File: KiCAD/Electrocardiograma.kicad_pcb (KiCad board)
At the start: 2 copper layers, 56.5 x 47.2 mm, 76 parts, among them J1 54-00174, J2 Conn_01x02_Pin, J3 USB_C_Receptacle_PowerOnly_6P, J4 Conn_01x02_Pin, J5 Conn_01x02_Pin, J6 Conn_01x04_Pin, U1 INA823DT, U2 ESP32-C3-WROOM-02, U3 TLV1117-33, U4 TLV4888, U5 TLV4888, U6 TLV1117-ADJ, U7 SC6038, U8 CH224K

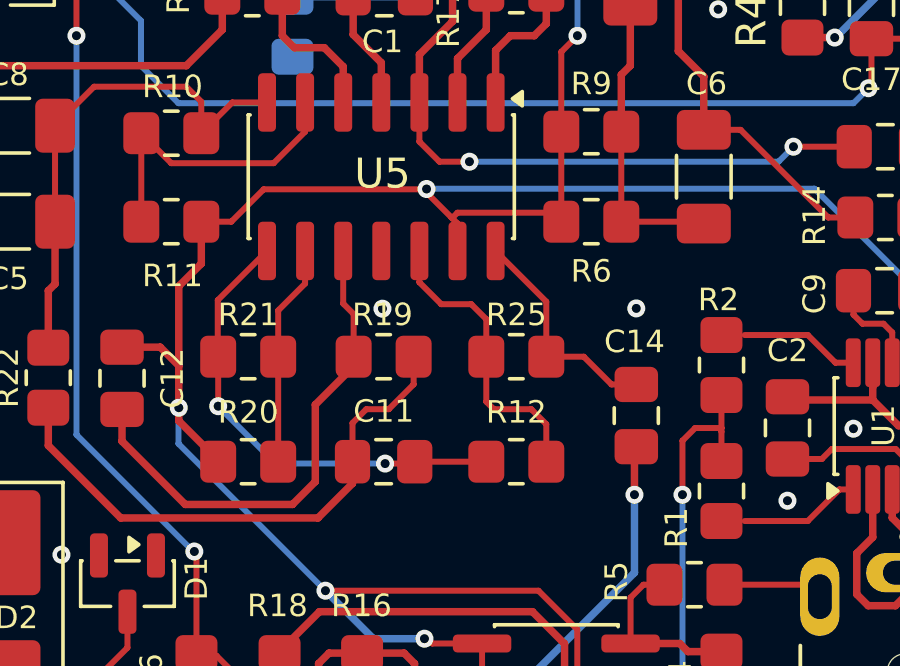
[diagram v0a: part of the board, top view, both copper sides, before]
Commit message: Corrección opamp
Corregido un opamp mal trazado en el esquematico y pcb
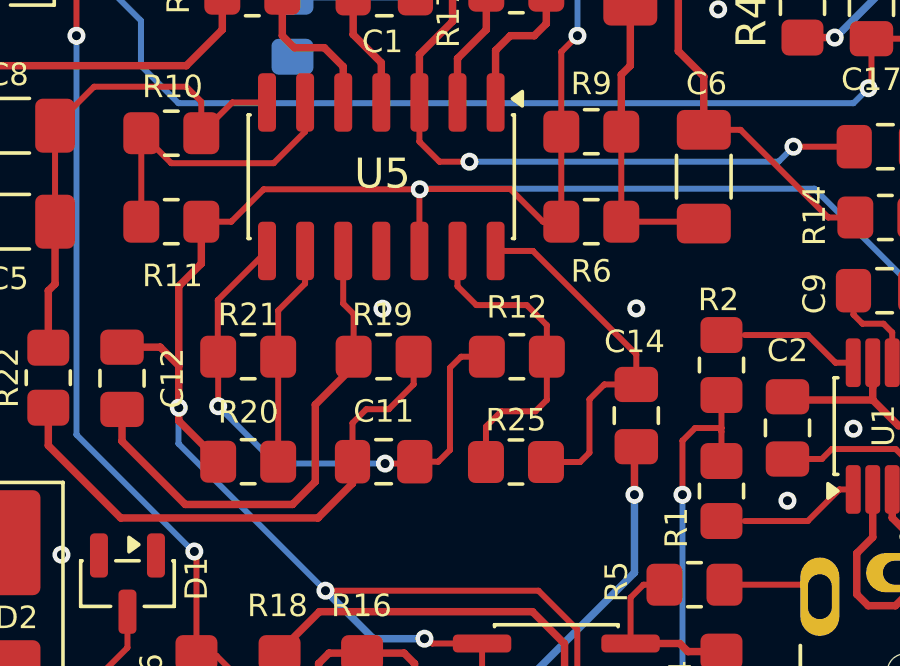
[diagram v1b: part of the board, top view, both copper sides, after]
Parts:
- moved R25 3.51 mm to (162.2, 104.2)
- moved R12 3.50 mm to (162.3, 100.7)
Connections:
- R12 pad 2: Net-(U5D-+) -> Net-(U5D--)
- R25 pad 1: Net-(U5D-+) -> Net-(U5D--)
- U5 pad 12: Net-(U5D-+) -> GND
- U5 pad 13: GND -> Net-(U5D--)
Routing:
- net Net-(U5D--): track 0.00 -> 10.8 mm
- net Net-(U5D-+): track 10.6 -> 0.00 mm
- net /Sensing_Out: track 7.81 -> 12.2 mm
- net /LPF_out: track 15.7 -> 18.8 mm
- net GND: track 95.0 -> 95.8 mm

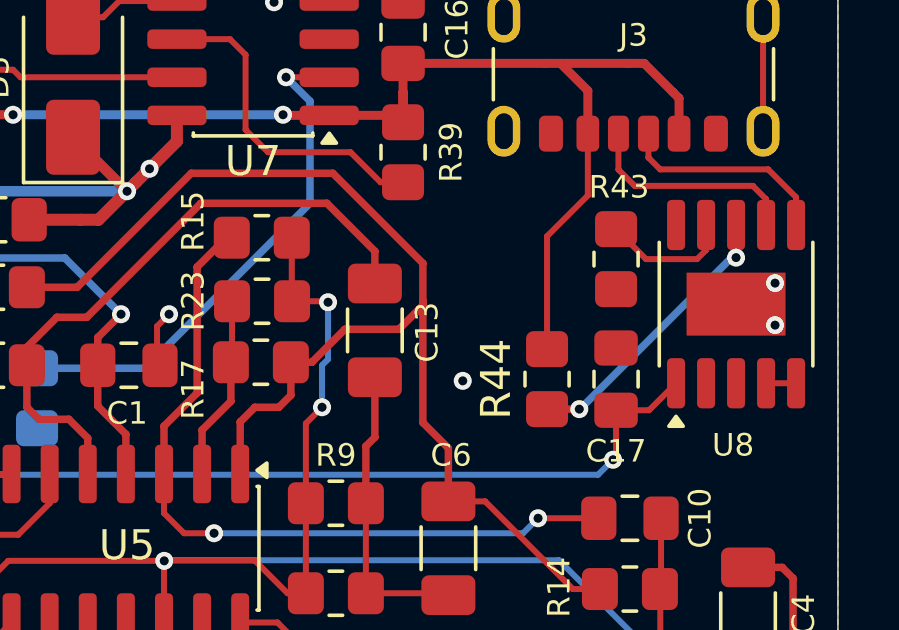
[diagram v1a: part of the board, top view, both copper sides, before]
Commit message: Added Charging indicator LED
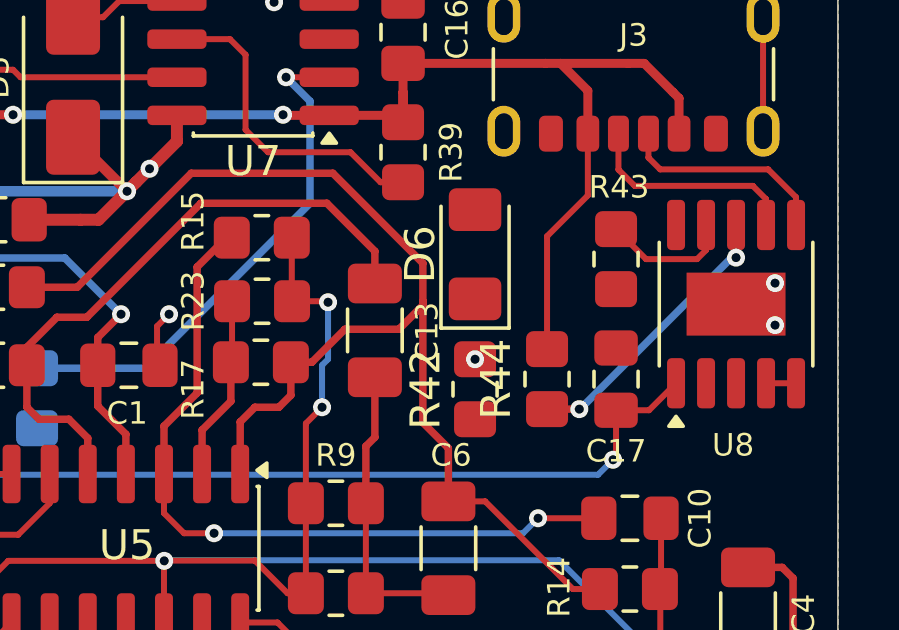
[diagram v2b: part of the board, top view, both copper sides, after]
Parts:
- added D6: LED, LED_SMD:LED_1206_3216Metric_Pad1.42x1.75mm_HandSolder, F.Cu at (169.4, 84.9)
- added R42: 470, Resistor_SMD:R_0805_2012Metric_Pad1.20x1.40mm_HandSolder, F.Cu at (169.4, 89.4)
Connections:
- U7 pad 3: unconnected-(U7-CHRG-Pad3) -> Net-(D6-A)

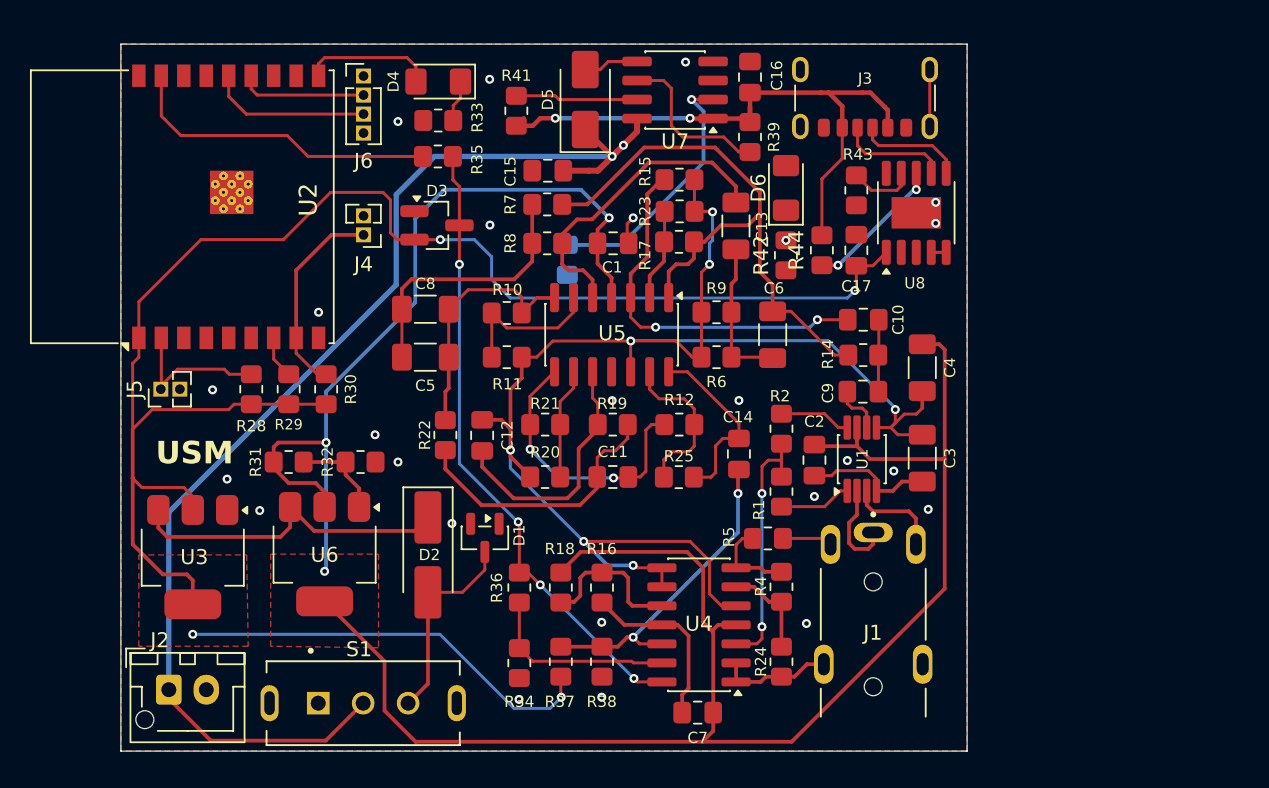
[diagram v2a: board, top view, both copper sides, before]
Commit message: Added new dimensions references and vias
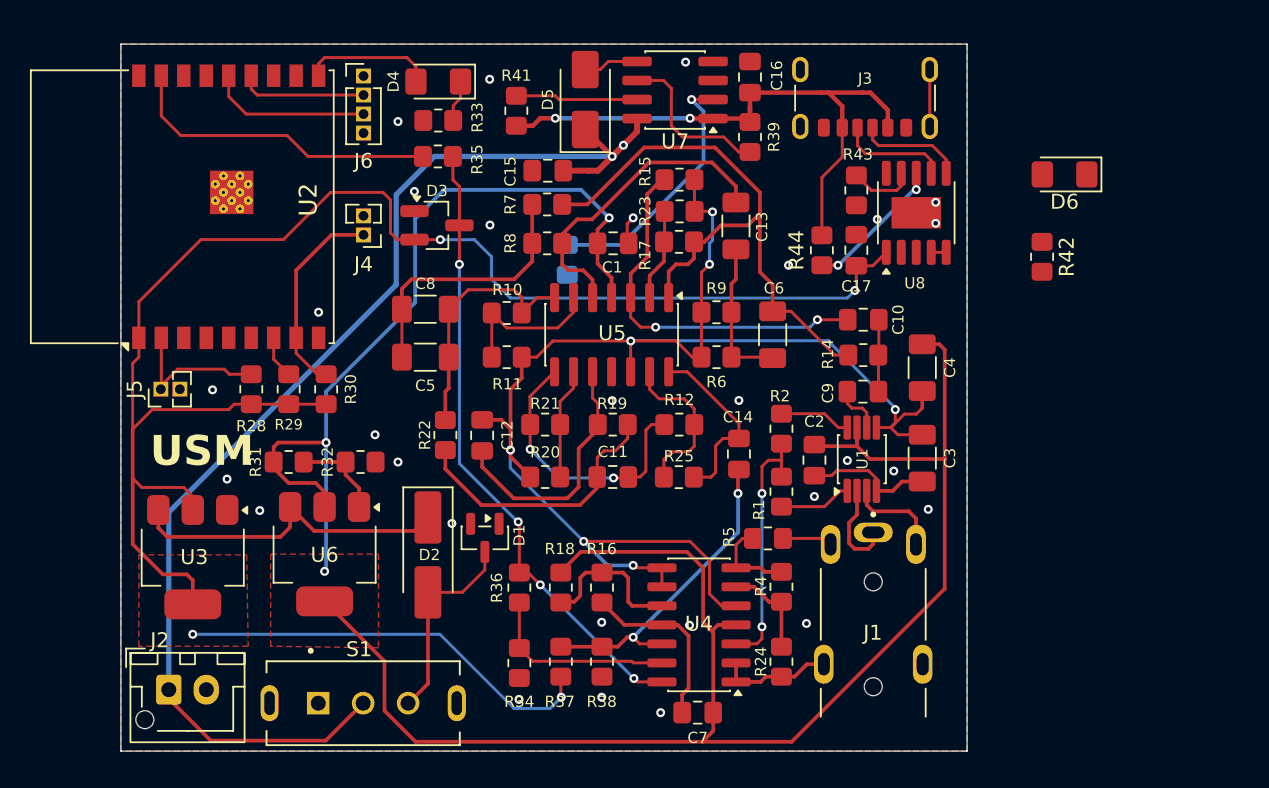
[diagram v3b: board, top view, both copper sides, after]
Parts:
- moved D6 18.6 mm to (188.0, 84.0), turned to 180 degrees
- moved R42 17.1 mm to (186.5, 89.5), turned to -90 degrees
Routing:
- net /Vbus: track 40.9 -> 40.2 mm
- net -BATT_REG: vias 25 -> 29

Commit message: Update Electrocardiograma.kicad_pcb
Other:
- board text added: "Nodo Negativo de OpAmps de filtrado, deben poseer la menor capacitancia a tierra parásita posible"
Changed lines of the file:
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@@
+		)
+	)
+	(gr_text "Nodo Negativo de OpAmps de filtrado, deben poseer\nla menor capacitancia a tierra parásita posible\n"
+		(at 120.5 62.5 0)
+		(layer "Cmts.User")
+		(effects
+			(font
+				(size 1.5 1.5)
+				(thickness 0.3)
+				(bold yes)
+			)
+			(justify left bottom)
 		)
 	)

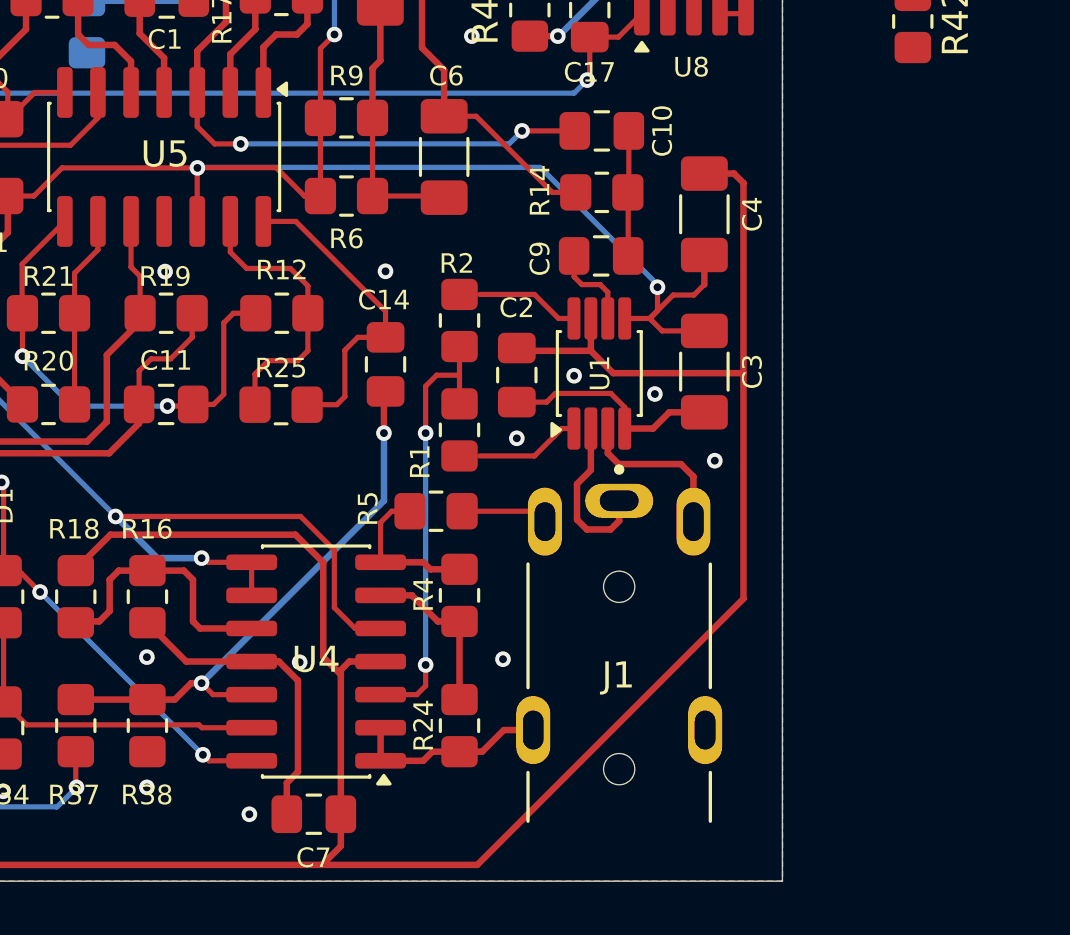
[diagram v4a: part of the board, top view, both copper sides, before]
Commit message: PCB traces and schematics connections corrected and
Rerouted the jack 3.5 connections to be consistent with the signals from the male connector.
Changed the 100nF load capacitors for the GND opamp, for 10uF decoupling capacitors in the tension divider of the same opamp.
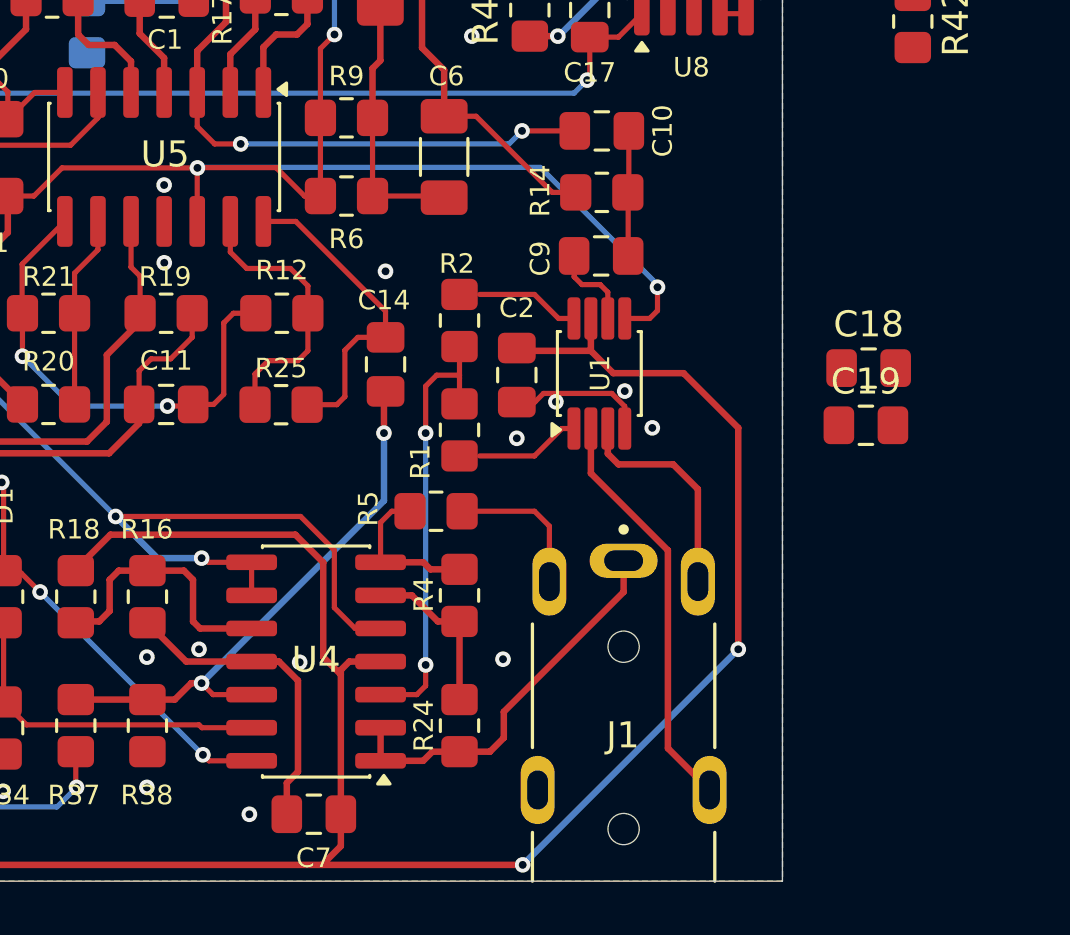
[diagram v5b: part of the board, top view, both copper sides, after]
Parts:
- removed C3, C4: 100n, Capacitor_SMD:C_1206_3216Metric_Pad1.33x1.80mm_HandSolder
- added C18: 10uF, Capacitor_SMD:C_0805_2012Metric_Pad1.18x1.45mm_HandSolder, F.Cu at (184.8, 102.8)
- added C19: 10uF, Capacitor_SMD:C_0805_2012Metric_Pad1.18x1.45mm_HandSolder, F.Cu at (184.7, 105.0)
- moved J1 2.31 mm to (175.4, 117.0)
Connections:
- J1 pad 1: Net-(U1--) -> Net-(U4A--)
- J1 pad 4_1: Net-(U4A--) -> unconnected-(J1-Pad4_1)
- J1 pad 4_2: unconnected-(J1-Pad4_2) -> Net-(U1--)
- R16 pad 2: Net-(U4C-+) -> Net-(R16-Pad2)
- R18 pad 1: Net-(U4C-+) -> Net-(R16-Pad2)
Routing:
- net Net-(U1--): track 6.40 -> 15.8 mm
- net +6.1V: track 161.4 -> 152.2 mm, vias 3 -> 5
- net Net-(U4A--): track 7.62 -> 15.1 mm
- net GND: track 95.8 -> 89.7 mm
- net -BATT_REG: track 27.9 -> 24.6 mm, vias 29 -> 31
- net Net-(J1-Pad2): track 3.34 -> 5.72 mm
- net Net-(U1-+): track 6.34 -> 8.54 mm
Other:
- board text added: "V2"

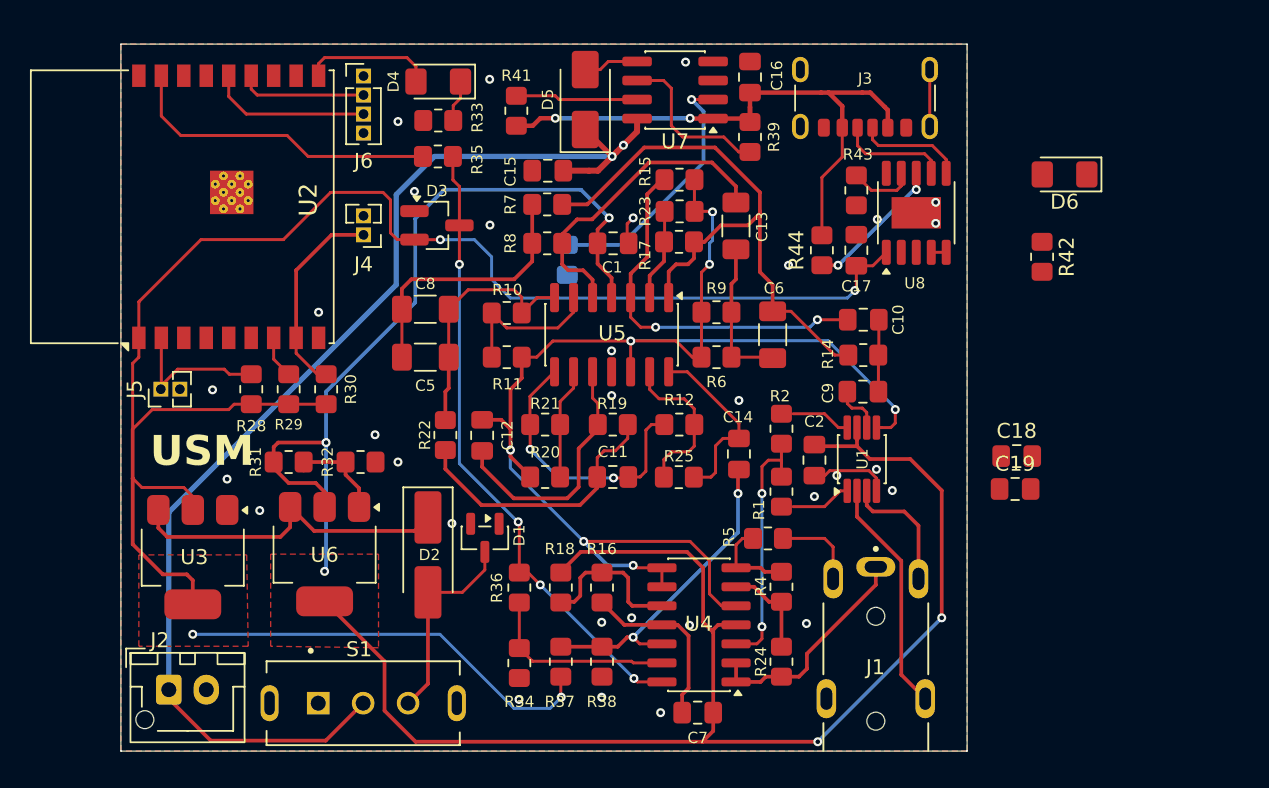
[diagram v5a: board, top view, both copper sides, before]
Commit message: Nueva version de la placa, se hicieron pequeños cambios
Cambios en el Esquematico y PCB
se añadieron capacitores de 10nF, valor que está por calcularse
añadí espaciado de margen al USB-C
Meandros al cable de entrada al Amplificador Instrumental
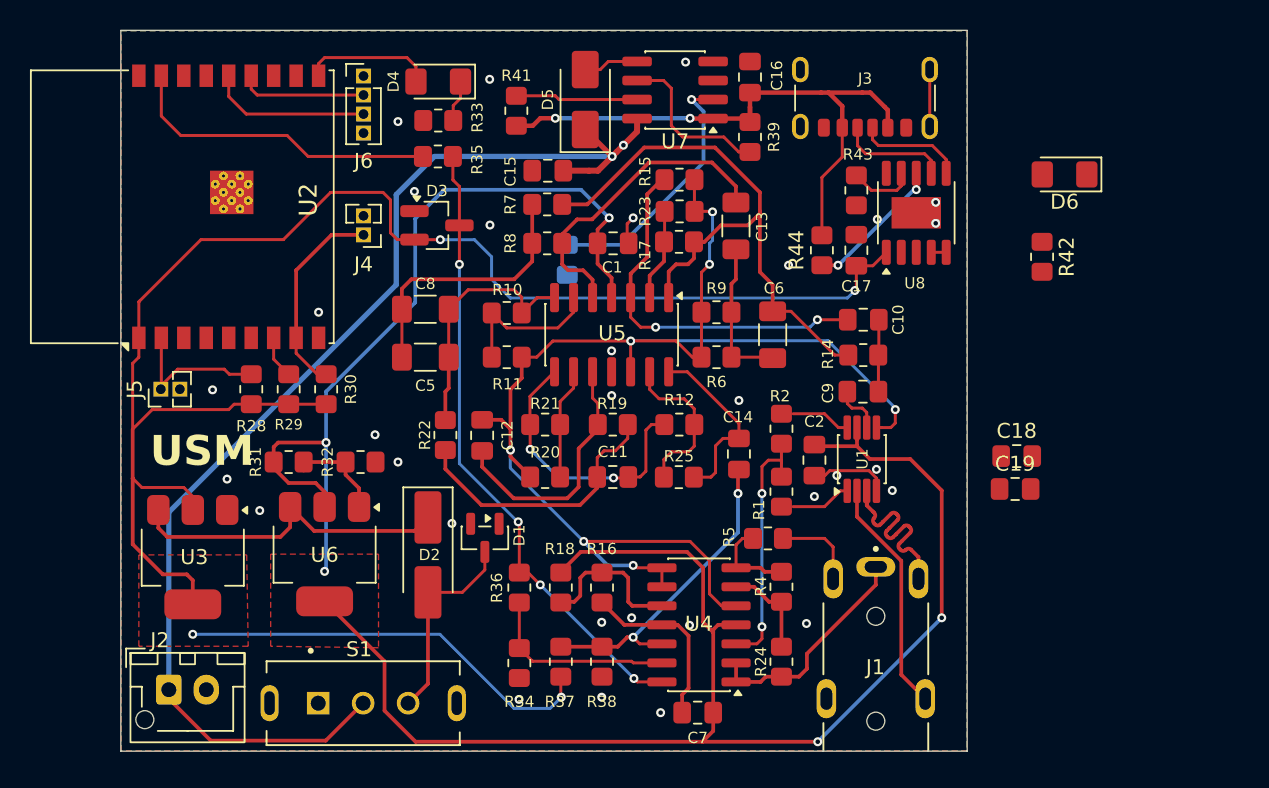
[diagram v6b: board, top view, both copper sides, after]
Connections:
- R16 pad 2: Net-(R16-Pad2) -> Net-(U4C-+)
- R18 pad 1: Net-(R16-Pad2) -> Net-(U4C-+)
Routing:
- net Net-(U1-+): track 8.54 -> 13.0 mm
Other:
- board size 56.5 x 47.2 mm -> 56.5 x 48.1 mm
- board text added: "Mantener margen para que USB-C no quede al aire"

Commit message: Orden y purga de simulaciónes, ademas se añadieron las footprints faltantes
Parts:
- added C20: 10nF, Capacitor_SMD:C_0805_2012Metric_Pad1.18x1.45mm_HandSolder, F.Cu at (197.0, 91.5)
- added C21: 10nF, Capacitor_SMD:C_0805_2012Metric_Pad1.18x1.45mm_HandSolder, F.Cu at (196.9, 94.5)
- added C22: 10nF, Capacitor_SMD:C_0805_2012Metric_Pad1.18x1.45mm_HandSolder, F.Cu at (196.9, 97.5)
- added C23: 10nF, Capacitor_SMD:C_0805_2012Metric_Pad1.18x1.45mm_HandSolder, F.Cu at (196.9, 100.5)
- added C24: 10nF, Capacitor_SMD:C_0805_2012Metric_Pad1.18x1.45mm_HandSolder, F.Cu at (196.9, 103.5)
- added C25: 10nF, Capacitor_SMD:C_0805_2012Metric_Pad1.18x1.45mm_HandSolder, F.Cu at (187.0, 107.5)
- D2: footprint Diode_SMD:D_SMA_Handsoldering -> Diode_SMD:D_SMA
- moved C19 34.7 mm to (152.0, 116.5), turned to -90 degrees
- moved C18 33.9 mm to (152.0, 111.5), turned to -90 degrees
- moved D1 5.11 mm to (145.0, 105.5), turned to 0 degrees
- moved R34 2.10 mm to (149.5, 116.5)
- moved R36 2.10 mm to (149.5, 111.5)
- moved D2 1.60 mm to (145.5, 111.0)
- moved C7 0.57 mm to (163.5, 120.5)
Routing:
- net Net-(U4C-+): track 10.2 -> 17.0 mm
- net +BATT: track 14.1 -> 18.7 mm
- net +6.1V: track 152.2 -> 156.5 mm
- net Net-(U4D--): track 12.9 -> 15.1 mm
- net /Leveled_Signal: track 42.1 -> 43.3 mm
- net -BATT_REG: track 24.6 -> 25.5 mm, vias 31 -> 32
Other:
- board text added: "Añadidos Capacitores de desacople"
- board text added: "Falso, debe sobresalir para igualar el grosor de la carcasa"
